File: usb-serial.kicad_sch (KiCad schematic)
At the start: 41 parts, among them J2 DB25_Plug, U1 ACPL-M50L, U10 TDR2-1222WI, U11 PEME2-5-D12-D, U2 ACPL-M50L, U3 USBLC6-2SC6, U4 ACPL-M50L, U5 ACPL-M50L, U6 Interface_USB_CP2102N-A01-GQF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, U7 SN75155, U8 SN75155, U9 LM1117DT-5.0

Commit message: Add fabrication fies
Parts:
- F1: value Polyfuse -> Polyfuse 1,8A; footprint Fuse:Fuse_0805_2012Metric -> Fuse:Fuse_1206_3216Metric
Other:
- note added: "C70081"
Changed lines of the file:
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@@
+    (effects (font (size 1.27 1.27)) (justify left bottom))
+  )
+  (text "C70081" (at 81.28 138.43 0)
     (effects (font (size 1.27 1.27)) (justify left bottom))
   )
@@
       (effects (font (size 1.27 1.27)))
     )
-    (property "Value" "Polyfuse" (at 81.28 142.24 90)
+    (property "Value" "Polyfuse 1,8A" (at 81.28 142.24 90)
       (effects (font (size 1.27 1.27)))
     )
-    (property "Footprint" "Fuse:Fuse_0805_2012Metric" (at 76.2 139.7 0)
+    (property "Footprint" "Fuse:Fuse_1206_3216Metric" (at 76.2 139.7 0)
       (effects (font (size 1.27 1.27)) (justify left) hide)
     )

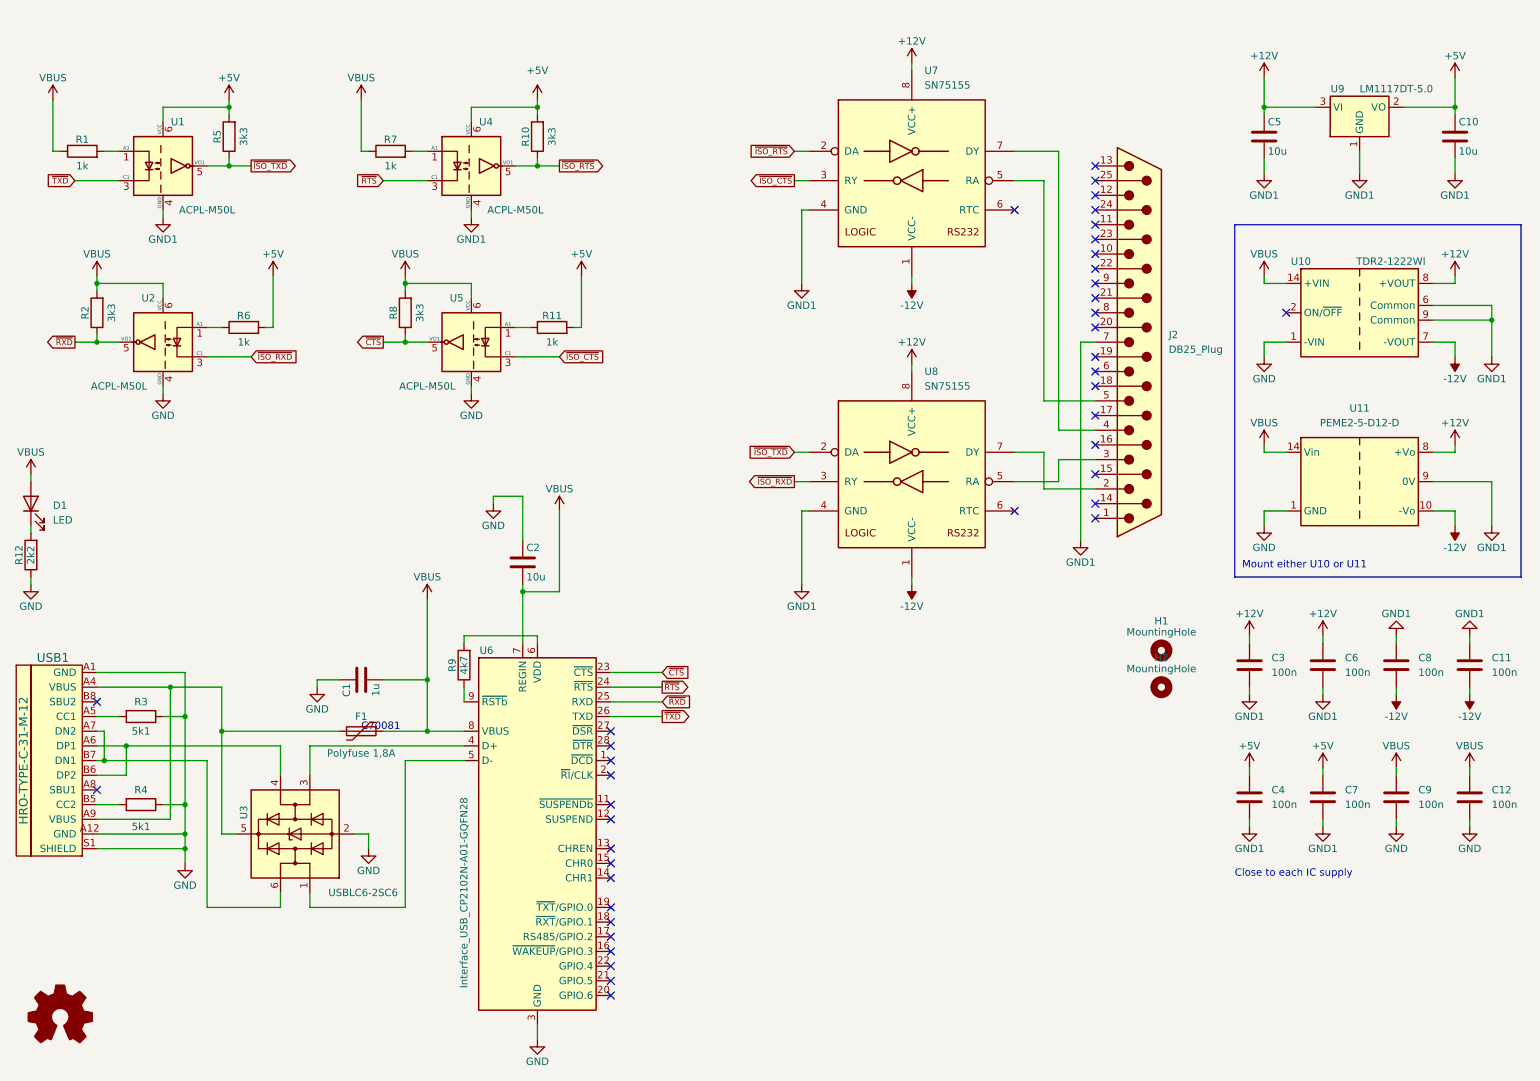
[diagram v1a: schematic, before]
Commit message: EMC filter according to DC/DC datasheet
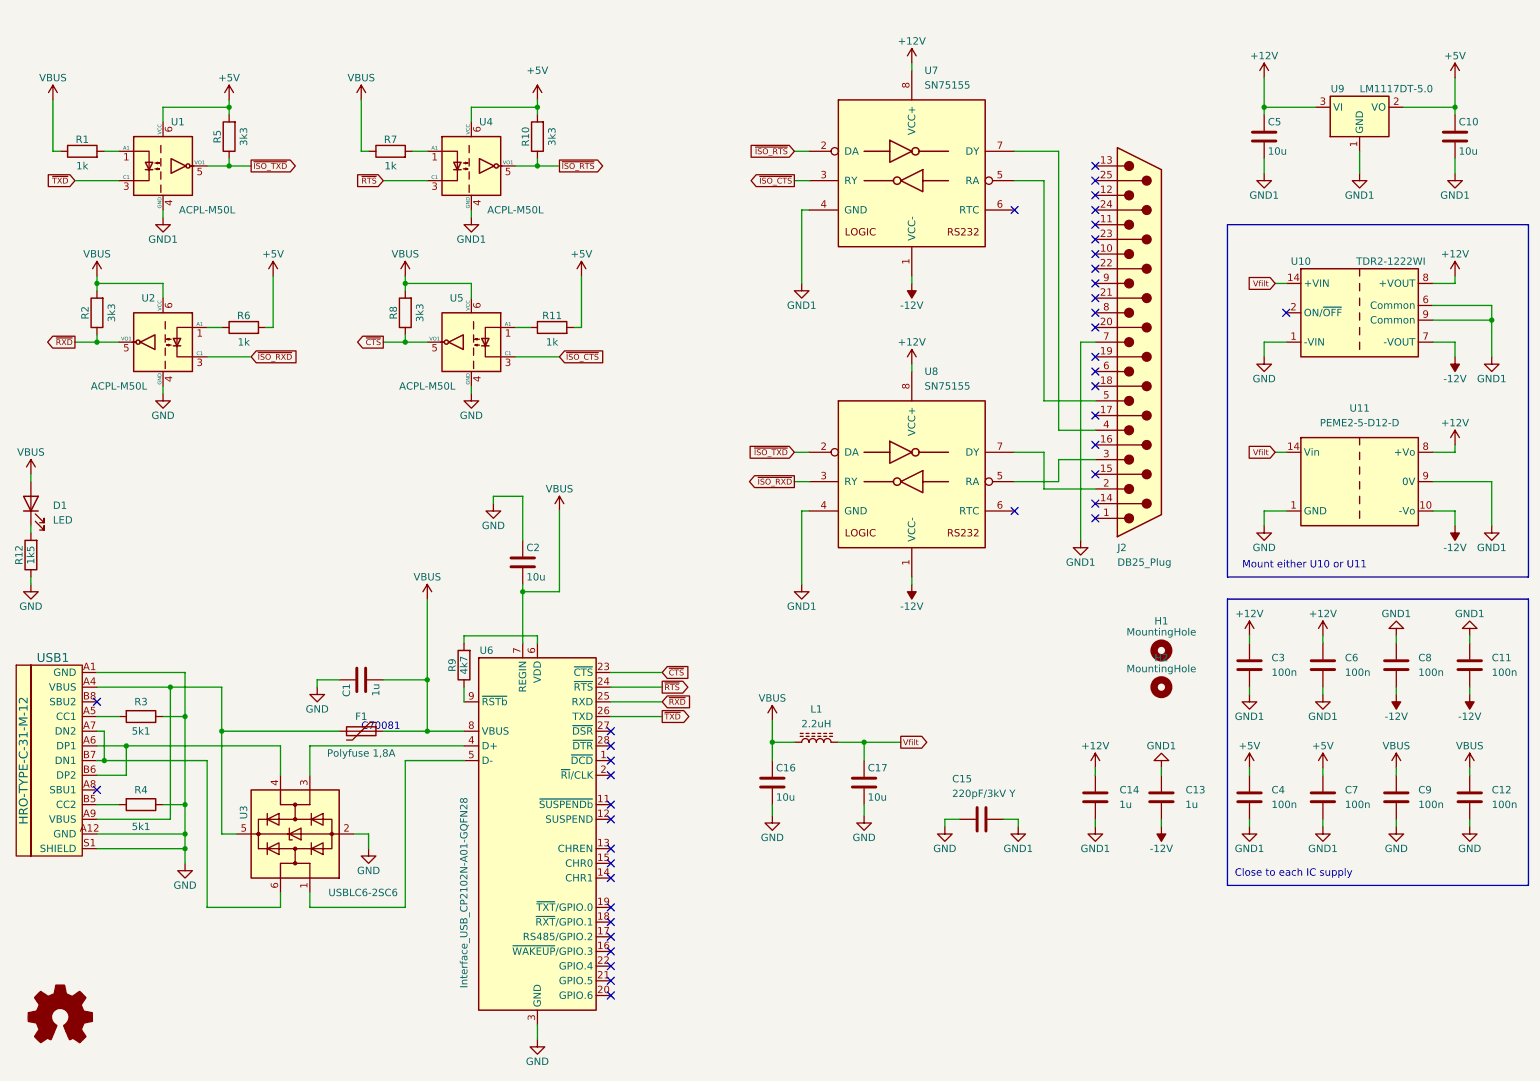
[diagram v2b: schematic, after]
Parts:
- added C13, C14: 1u, Capacitor_SMD:C_0805_2012Metric, symbol Device:C
- added C15: 220pF/3kV Y, Capacitor_SMD:C_1812_4532Metric, symbol Device:C
- added C16, C17: 10u, Capacitor_SMD:C_0805_2012Metric, symbol Device:C
- added L1: 2.2uH, Inductor_SMD:L_6.3x6.3_H3, symbol Device:L_Ferrite
- R12: value 2k2 -> 1k5
- U7, U8: footprint Package_SO:SO-8_5.3x6.2mm_P1.27mm -> Package_SO:SO-8_3.9x4.9mm_P1.27mm
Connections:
- net +12V: now also C14.2
- net -12V: now also C13.1
- net GND: now also C15.2, C16.2, C17.2
- net GND1: now also C13.2, C14.1, C15.1
- net VBUS: now also C16.1, L1.1; no longer U10.14 (+VIN), U11.14 (Vin)
- new net Vfilt: C17.1, L1.2, U10.14 (+VIN), U11.14 (Vin)

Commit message: usb-serial: Change opto to MAX 22246 isolator.
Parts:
- removed R1, R11, R6, R7: 1k, Resistor_SMD:R_0402_1005Metric, symbol Device:R
- removed R10, R2, R5, R8: 3k3, Resistor_SMD:R_0402_1005Metric, symbol Device:R
- removed U1, U2, U4, U5: ACPL-M50L, Package_SO:SO-5_4.4x3.6mm_P1.27mm, symbol anders:ACPL-M50L
- added C18: 220pF/3kV Y, Capacitor_SMD:C_1812_4532Metric, symbol Device:C
- added U12, U13: MAX22246, anders:MAX22246, symbol anders:MAX22246
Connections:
- net +5V: now also U12.8 (VDDB), U13.8 (VDDB)
- net GND: now also C18.2, U12.4 (GNDA), U13.4 (GNDA)
- net GND1: now also C18.1, U12.5 (GNDB), U13.5 (GNDB)
- net VBUS: no longer C12.1, C9.1
- net ~{CTS}: now also U13.2 (OUT1)
- net ~{ISO_CTS}: now also U13.7 (IN1)
- net ~{ISO_RTS}: now also U13.6 (OUT2)
- net ~{ISO_RXD}: now also U12.7 (IN1)
- net ~{ISO_TXD}: now also U12.6 (OUT2)
- net ~{RTS}: now also U13.3 (IN2)
- net ~{RXD}: now also U12.3 (IN2)
- net ~{TXD}: now also U12.2 (OUT1)
- net +3.3V: now reaches R9.2, U6.6 (VDD)
- net +3.3V: now also C12.1, C9.1, U12.1 (VDDA), U13.1 (VDDA)
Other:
- title: Opto isolated USB to RS232 converter -> Isolated USB to RS232 converter
- moved on the sheet: C15, H2

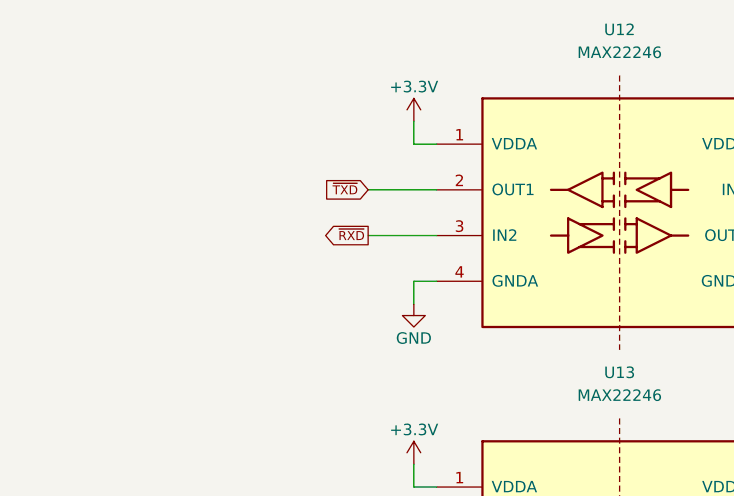
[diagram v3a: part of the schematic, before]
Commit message: usb-serial: Fix swapped RXD and TXD
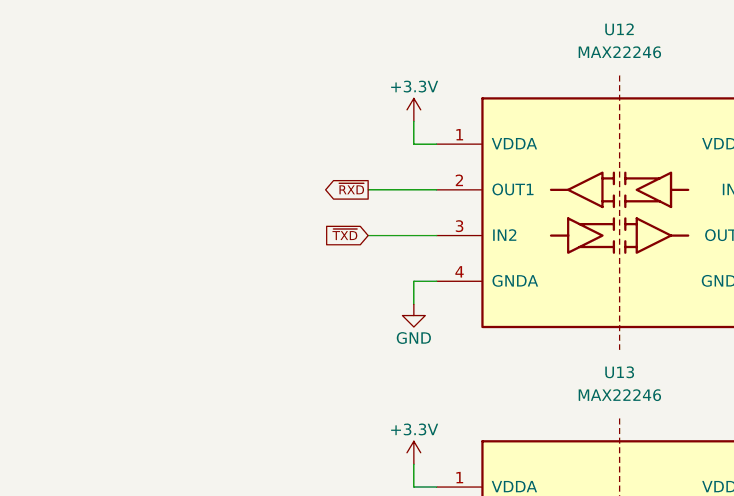
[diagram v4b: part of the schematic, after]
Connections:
- net ~{RXD}: now also U12.2 (OUT1); no longer U12.3 (IN2)
- net ~{TXD}: now also U12.3 (IN2); no longer U12.2 (OUT1)

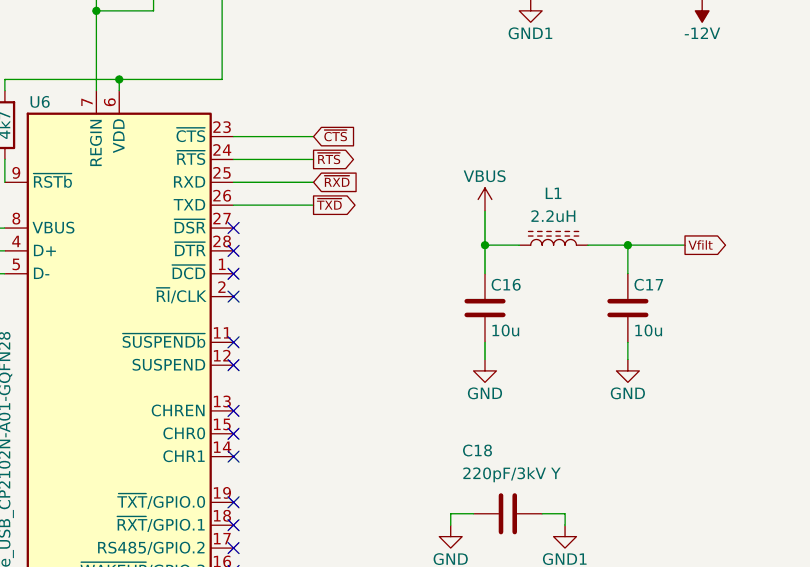
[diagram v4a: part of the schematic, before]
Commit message: Add resistor to fix serial break support
There must be pulldown resistor of 10k from TxD to GND on the CP2102 to
make serial break to work.

Also, updated to use KiCad 9.0 as PCB design tool.
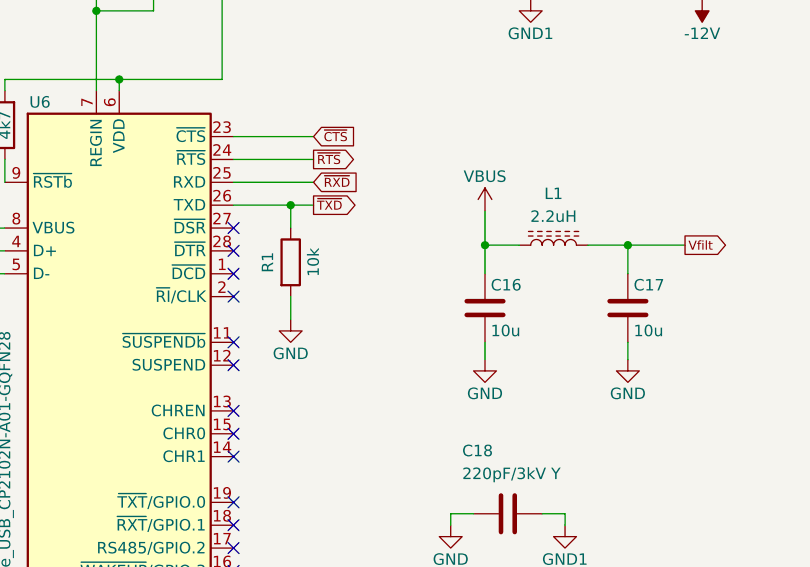
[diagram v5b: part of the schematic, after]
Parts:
- added R1: 10k, Resistor_SMD:R_0402_1005Metric, symbol Device:R
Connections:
- net GND: now also R1.2
- net ~{TXD}: now also R1.1
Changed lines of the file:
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@@
 (kicad_sch
-	(version 20231120)
+	(version 20250114)
 	(generator "eeschema")
-	(generator_version "8.0")
+	(generator_version "9.0")
 	(paper "A4")
 	(title_block
 		(title "Isolated USB to RS232 converter")
-		(rev "2")
+		(rev "3")
 		(company "Anders Sandahl")
 	)
+	(rectangle
+		(start 231.14 115.57)
+		(end 283.21 165.1)
+		(stroke
+			(width 0)
+			(type default)
+		)
+		(fill
+			(type none)
+		)
+	)
+	(rectangle
+		(start 231.14 50.8)
+		(end 283.21 111.76)
+		(stroke
+			(width 0)
+			(type default)
+		)
+		(fill
+			(type none)
+		)
+	)
+	(rectangle
+		(start 232.41 50.8)
+		(end 232.41 50.8)
+		(stroke
+			(width 0)
+			(type default)
+		)
+		(fill
+			(type none)
+		)
+	)
+	(text "Close to each IC supply"
+		(exclude_from_sim no)
+		(at 232.41 163.83 0)
+		(effects
+			(font
+				(size 1.27 1.27)
+			)
+			(justify left bottom)
+		)
+	)
+	(text "C70081"
+		(exclude_from_sim no)
+		(at 81.28 138.43 0)
+		(effects
+			(font
+				(size 1.27 1.27)
+			)
+			(justify left bottom)
+		)
+	)
+	(text "Mount either U10 or U11"
+		(exclude_from_sim no)
+		(at 233.68 110.49 0)
+		(effects
+			(font
+				(size 1.27 1.27)
+			)
+			(justify left bottom)
+		)
+	)
 	(junction
 		(at 109.22 114.3)
@@
 	)
 	(junction
+		(at 130.81 135.89)
+		(diameter 0)
+		(color 0 0 0 0)
+	)
+	(junction
 		(at 36.83 143.51)
 		(diameter 0)
@@
 	(wire
 		(pts
+			(xy 130.81 146.05) (xy 130.81 148.59)
+		)
+		(stroke
+			(width 0)
+			(type default)
+		)
+	)
+	(wire
+		(pts
 			(xy 266.7 95.25) (xy 276.86 95.25)
 		)
@@
 	(wire
 		(pts
+			(xy 130.81 135.89) (xy 133.35 135.89)
+		)
+		(stroke
+			(width 0)
+			(type default)
+		)
+	)
+	(wire
+		(pts
 			(xy 54.61 143.51) (xy 54.61 168.91)
 		)
@@
 	(wire
 		(pts
+			(xy 130.81 135.89) (xy 130.81 138.43)
+		)
+		(stroke
+			(width 0)
+			(type default)
+		)
+	)
+	(wire
+		(pts
 			(xy 35.56 128.27) (xy 50.8 128.27)
 		)
@@
 	(wire
 		(pts
-			(xy 124.46 135.89) (xy 133.35 135.89)
+			(xy 124.46 135.89) (xy 130.81 135.89)
 		)
 		(stroke
@@
 		)
 	)
-	(rectangle
-		(start 231.14 115.57)
-		(end 283.21 165.1)
-		(stroke
-			(width 0)
-			(type default)
-		)
-		(fill
-			(type none)
-		)
-	)
-	(rectangle
-		(start 231.14 50.8)
-		(end 283.21 111.76)
-		(stroke
-			(width 0)
-			(type default)
-		)
-		(fill
-			(type none)
-		)
-	)
-	(rectangle
-		(start 232.41 50.8)
-		(end 232.41 50.8)
-		(stroke
-			(width 0)
-			(type default)
-		)
-		(fill
-			(type none)
-		)
-	)
-	(text "Close to each IC supply"
-		(exclude_from_sim no)
-		(at 232.41 163.83 0)
-		(effects
-			(font
-				(size 1.27 1.27)
-			)
-			(justify left bottom)
-		)
-	)
-	(text "C70081"
-		(exclude_from_sim no)
-		(at 81.28 138.43 0)
-		(effects
-			(font
-				(size 1.27 1.27)
-			)
-			(justify left bottom)
-		)
-	)
-	(text "Mount either U10 or U11"
-		(exclude_from_sim no)
-		(at 233.68 110.49 0)
-		(effects
-			(font
-				(size 1.27 1.27)
-			)
-			(justify left bottom)
-		)
-	)
 	(global_label "Vfilt"
 		(shape input)
@@
 	(symbol
 		(lib_id "power:GND")
+		(at 130.81 148.59 0)
+		(unit 1)
+		(exclude_from_sim no)
+		(in_bom yes)
+		(on_board yes)
+		(dnp no)
+		(property "Reference" "#PWR04"
+			(at 130.81 154.94 0)
+			(effects
+				(font
+					(size 1.27 1.27)
+				)
+				(hide yes)
+			)
+		)
+		(property "Value" "GND"
+			(at 130.81 152.4 0)
+			(effects
+				(font
+					(size 1.27 1.27)
+				)
+			)
+		)
+		(property "Footprint" ""
+			(at 130.81 148.59 0)
+			(effects
+				(font
+					(size 1.27 1.27)
+				)
+				(hide yes)
+			)
+		)
+		(property "Datasheet" ""
+			(at 130.81 148.59 0)
+			(effects
+				(font
+					(size 1.27 1.27)
+				)
+				(hide yes)
+			)
+		)
+		(property "Description" ""
+			(at 130.81 148.59 0)
+			(effects
+				(font
+					(size 1.27 1.27)
+				)
+				(hide yes)
+			)
+		)
+		(pin "1"
+		)
+		(instances
+			(project "usb-serial"
+				(path "/45119d54-9bb4-41fa-943c-6e8d0ad5f7c8"
+					(reference "#PWR04")
+					(unit 1)
+				)
+			)
+		)
+	)
+	(symbol
+		(lib_id "power:GND")
 		(at 168.275 153.035 0)
 		(unit 1)
@@
 	)
 	(symbol
+		(lib_id "Device:R")
+		(at 130.81 142.24 0)
+		(unit 1)
+		(exclude_from_sim no)
+		(in_bom yes)
+		(on_board yes)
+		(dnp no)
+		(property "Reference" "R1"
+			(at 128.27 142.24 90)
+			(effects
+				(font
+					(size 1.27 1.27)
+				)
+			)
+		)
+		(property "Value" "10k"
+			(at 133.35 142.24 90)
+			(effects
+				(font
+					(size 1.27 1.27)
+				)
+			)
+		)
+		(property "Footprint" "Resistor_SMD:R_0402_1005Metric"
+			(at 129.032 142.24 90)
+			(effects
+				(font
+					(size 1.27 1.27)
+				)
+				(hide yes)
+			)
+		)
+		(property "Datasheet" "~"
+			(at 130.81 142.24 0)
+			(effects
+				(font
+					(size 1.27 1.27)
+				)
+				(hide yes)
+			)
+		)
+		(property "Description" ""
+			(at 130.81 142.24 0)
+			(effects
+				(font
+					(size 1.27 1.27)
+				)
+				(hide yes)
+			)
+		)
+		(pin "1"
+		)
+		(pin "2"
+		)
+		(instances
+			(project "usb-serial"
+				(path "/45119d54-9bb4-41fa-943c-6e8d0ad5f7c8"
+					(reference "R1")
+					(unit 1)
+				)
+			)
+		)
+	)
+	(symbol
 		(lib_id "Device:C")
 		(at 260.35 127 0)
@@
 		)
 	)
+	(embedded_fonts no)
 )
